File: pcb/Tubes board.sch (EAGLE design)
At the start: 5 parts, among them J2 MAIN POWER, J3 LED DAT, J4 LED POWER, M1 WIRELESS-NRF24L01

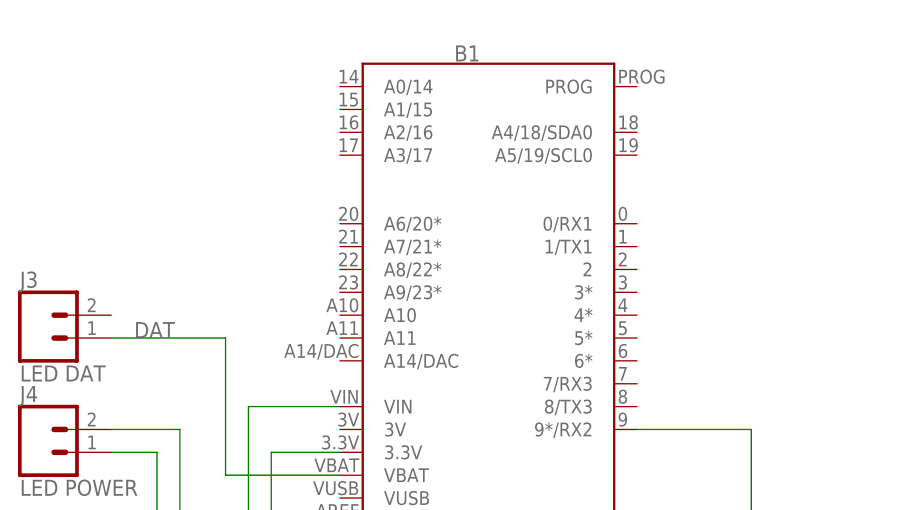
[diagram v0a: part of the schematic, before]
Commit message: Add missing wire
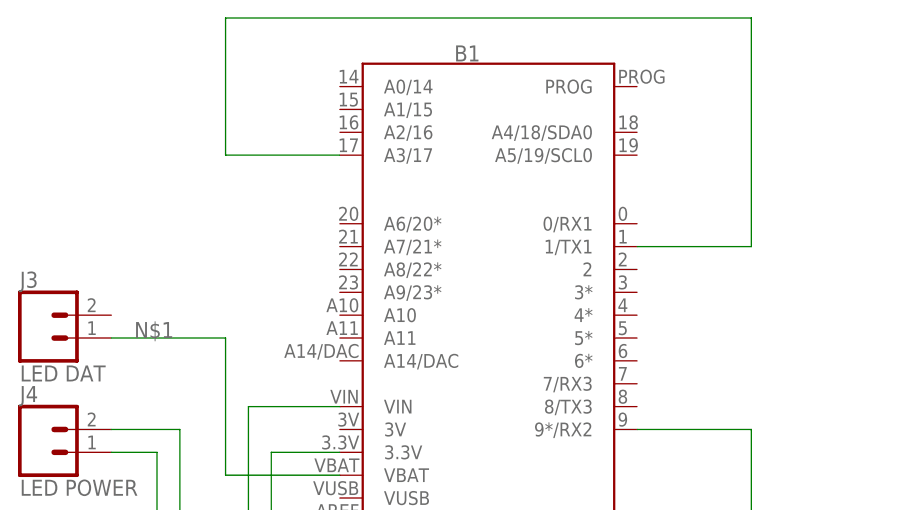
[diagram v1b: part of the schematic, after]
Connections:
- new net N$1: B1.VBAT, J3.1
- net DAT: now also B1.1/TX1, B1.A3/17; no longer B1.VBAT, J3.1
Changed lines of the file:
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@@
 <net name="DAT" class="0">
 <segment>
-<pinref part="J3" gate="G$1" pin="1"/>
-<wire x1="-10.16" y1="73.66" x2="2.54" y2="73.66" width="0.1524" layer="91"/>
-<wire x1="2.54" y1="73.66" x2="2.54" y2="58.42" width="0.1524" layer="91"/>
-<pinref part="B1" gate="G$1" pin="VBAT"/>
-<wire x1="2.54" y1="58.42" x2="15.24" y2="58.42" width="0.1524" layer="91"/>
-<label x="-7.62" y="73.66" size="1.778" layer="95"/>
+<pinref part="B1" gate="G$1" pin="1/TX1"/>
+<wire x1="48.26" y1="83.82" x2="60.96" y2="83.82" width="0.1524" layer="91"/>
+<wire x1="60.96" y1="83.82" x2="60.96" y2="109.22" width="0.1524" layer="91"/>
+<wire x1="60.96" y1="109.22" x2="2.54" y2="109.22" width="0.1524" layer="91"/>
+<wire x1="2.54" y1="109.22" x2="2.54" y2="93.98" width="0.1524" layer="91"/>
+<pinref part="B1" gate="G$1" pin="A3/17"/>
+<wire x1="15.24" y1="93.98" x2="2.54" y2="93.98" width="0.1524" layer="91"/>
 </segment>
 </net>
@@
 </segment>
 </net>
+<net name="N$1" class="0">
+<segment>
+<pinref part="B1" gate="G$1" pin="VBAT"/>
+<pinref part="J3" gate="G$1" pin="1"/>
+<wire x1="-10.16" y1="73.66" x2="2.54" y2="73.66" width="0.1524" layer="91"/>
+<wire x1="2.54" y1="73.66" x2="2.54" y2="58.42" width="0.1524" layer="91"/>
+<wire x1="2.54" y1="58.42" x2="15.24" y2="58.42" width="0.1524" layer="91"/>
+<label x="-7.62" y="73.66" size="1.778" layer="95"/>
+</segment>
+</net>

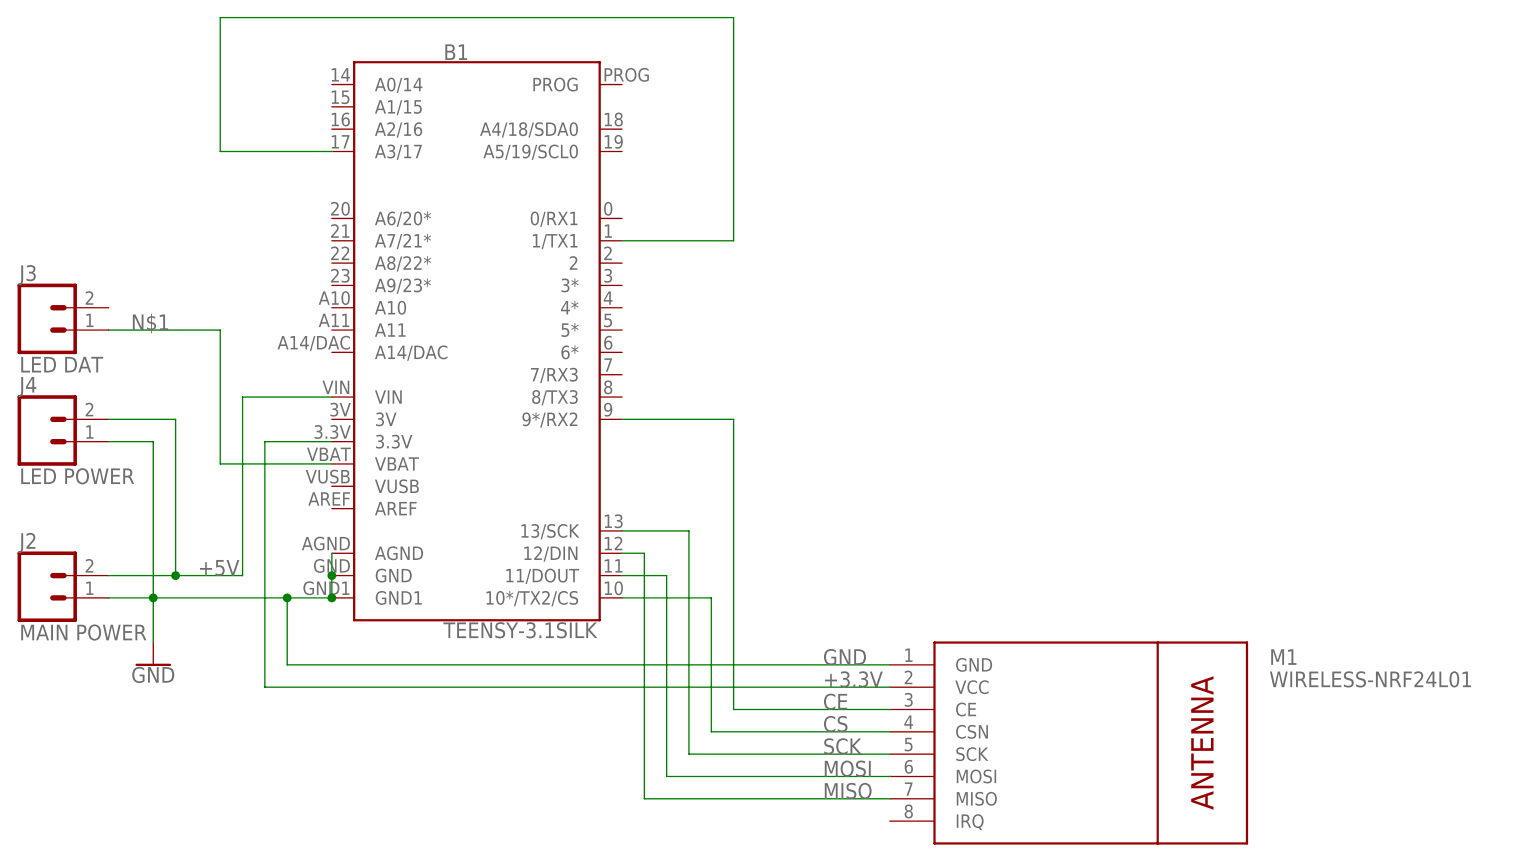
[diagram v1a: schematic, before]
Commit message: Wire IRQ
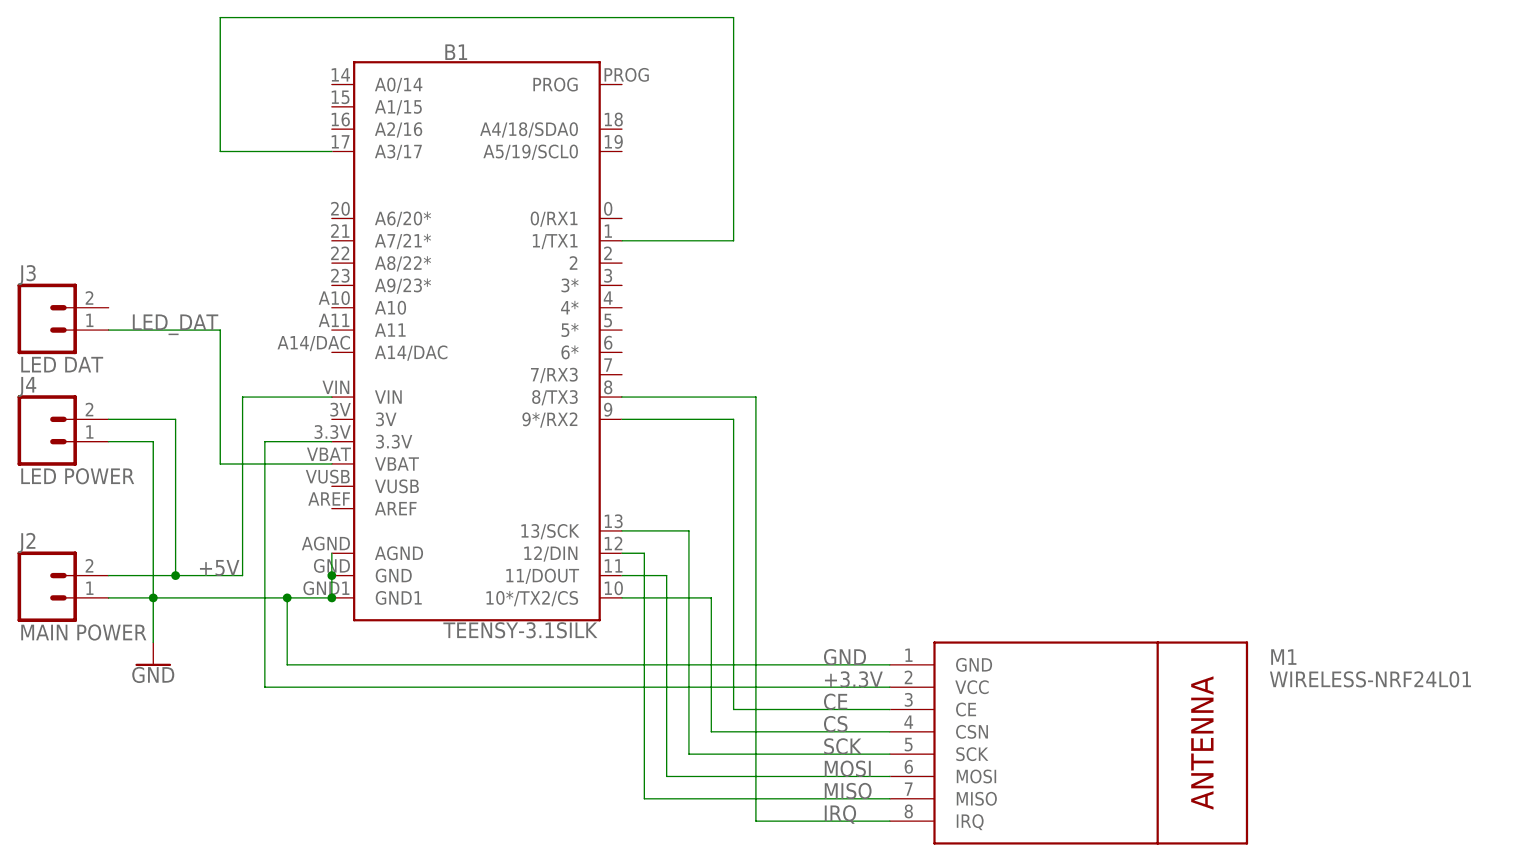
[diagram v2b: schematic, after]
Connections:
- net N$1 renamed LED_DAT
- new net IRQ: B1.8/TX3, M1.IRQ
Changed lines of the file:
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@@
 </segment>
 </net>
-<net name="N$1" class="0">
+<net name="LED_DAT" class="0">
 <segment>
 <pinref part="B1" gate="G$1" pin="VBAT"/>
@@
 </segment>
 </net>
+<net name="IRQ" class="0">
+<segment>
+<pinref part="M1" gate="G$1" pin="IRQ"/>
+<wire x1="78.74" y1="17.78" x2="63.5" y2="17.78" width="0.1524" layer="91"/>
+<pinref part="B1" gate="G$1" pin="8/TX3"/>
+<wire x1="63.5" y1="17.78" x2="63.5" y2="66.04" width="0.1524" layer="91"/>
+<wire x1="63.5" y1="66.04" x2="48.26" y2="66.04" width="0.1524" layer="91"/>
+<label x="71.12" y="17.78" size="1.778" layer="95"/>
+</segment>
+</net>
